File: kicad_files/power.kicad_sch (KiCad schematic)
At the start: 20 parts, among them J8 Conn_01x02_Socket, Q1 FDMC510P-MS, U11 LT1963AxST-3.3, U12 AP63205WU

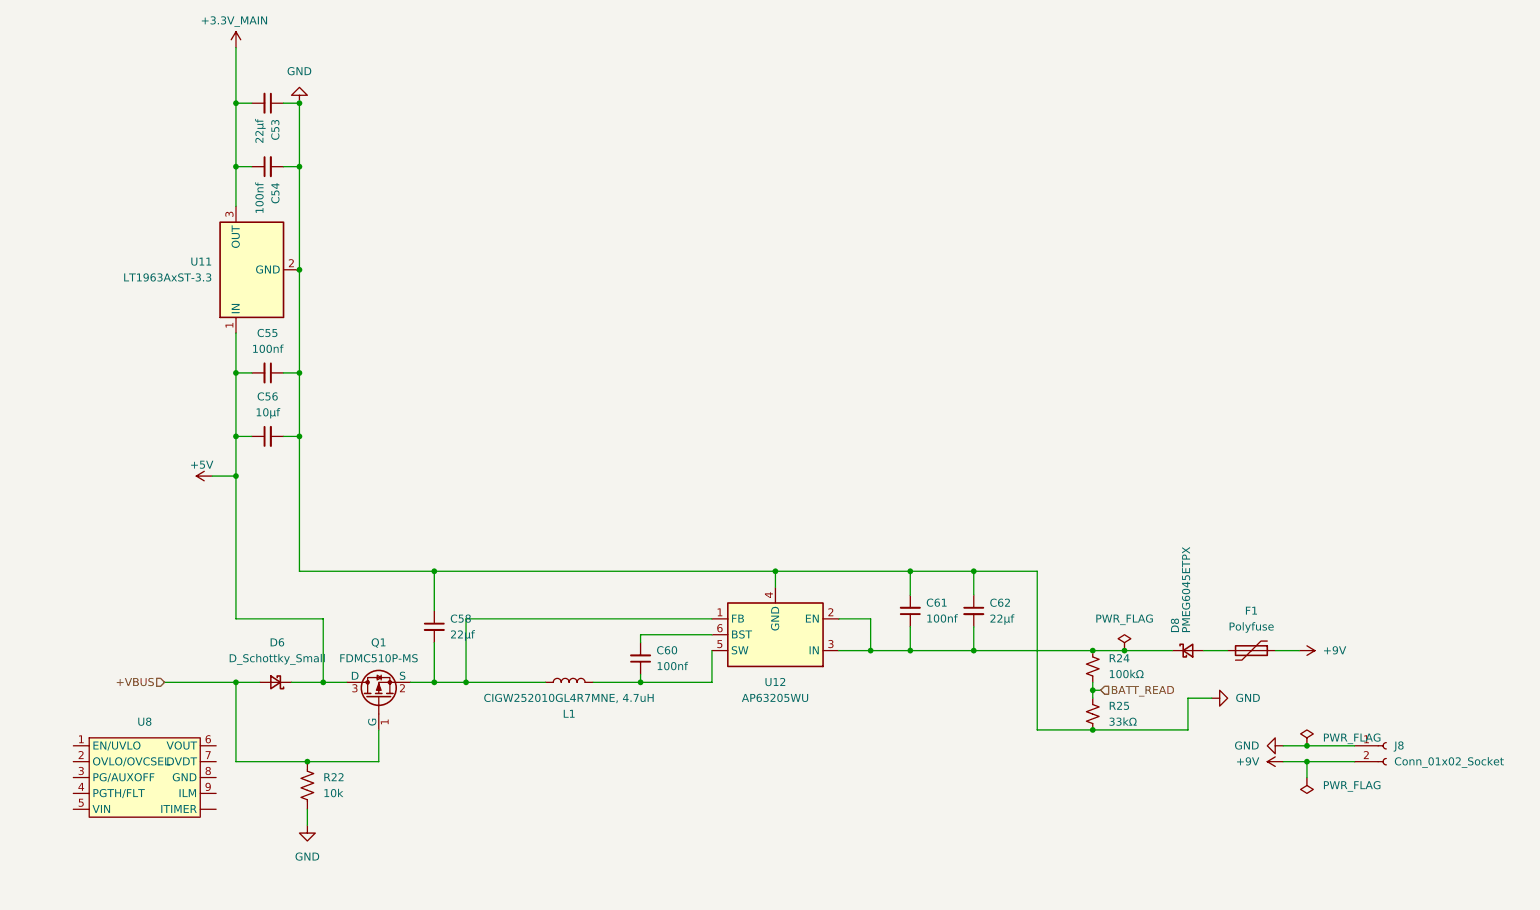
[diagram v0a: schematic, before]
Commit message: add dedicated power switching
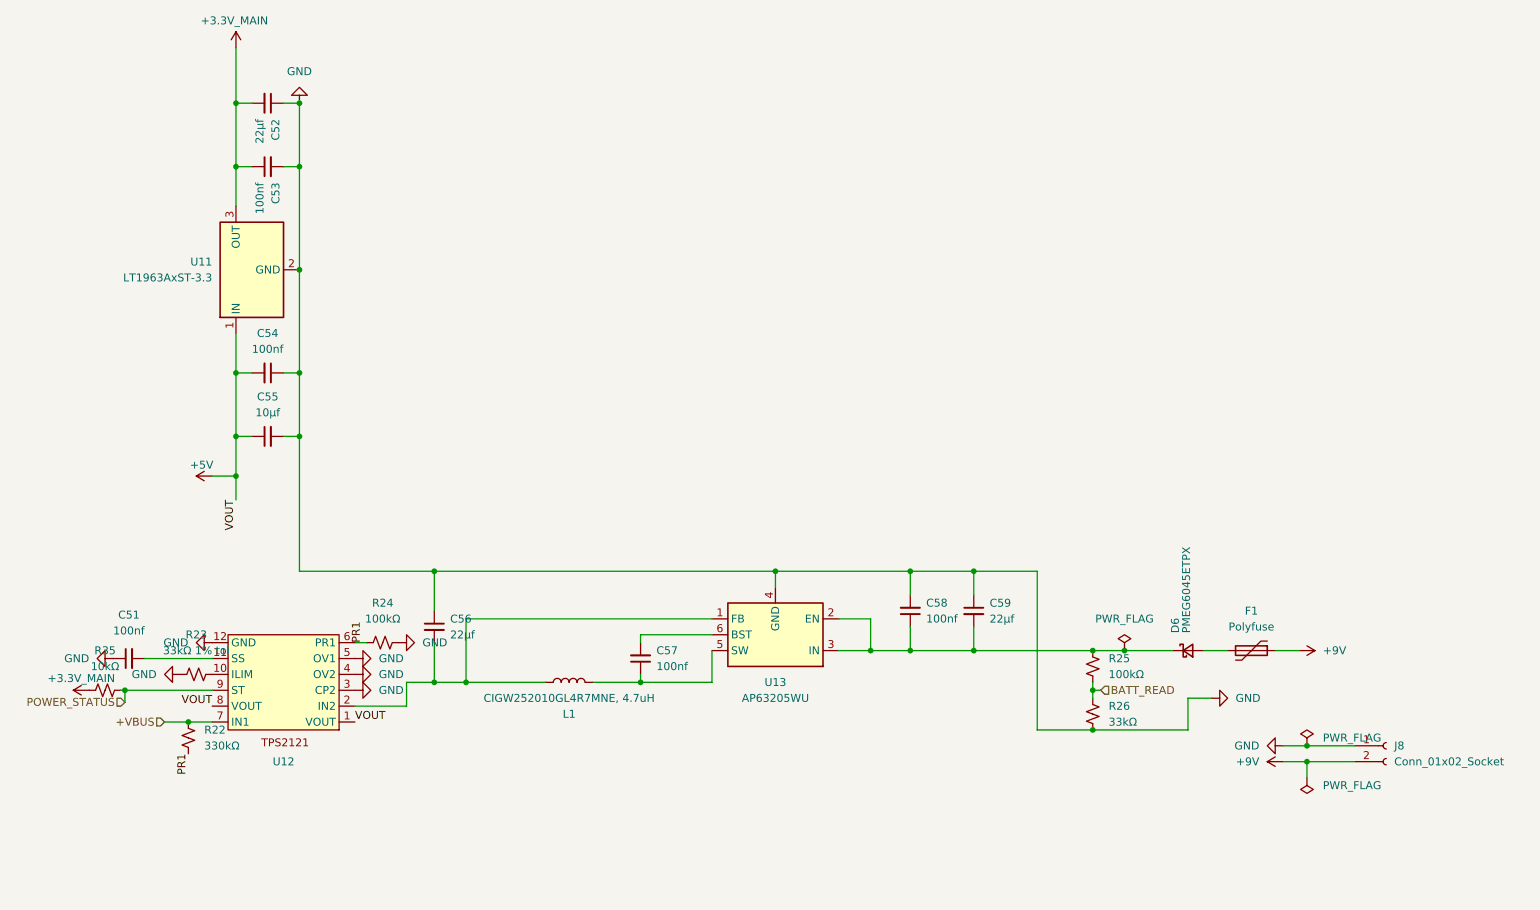
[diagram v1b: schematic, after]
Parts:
- removed D6: D_Schottky_Small, symbol Device:D_Schottky_Small
- removed Q1: FDMC510P-MS, Package_DFN_QFN:DFN-8-1EP_3x3mm_P0.65mm_EP1.6x2.56mm_ThermalVias, symbol Transistor_FET:Q_PMOS_GSD
- removed R22: 10k, Resistor_SMD:R_0402_1005Metric, symbol Device:R_US
- added C51: 100nf, Capacitor_SMD:C_0402_1005Metric, symbol Device:C_Small
- added R22: 330kΩ, Resistor_SMD:R_0402_1005Metric, symbol Device:R_Small_US
- added R23: 33kΩ 1% tol, Resistor_SMD:R_0402_1005Metric, symbol Device:R_Small_US
- added R24: 100kΩ, Resistor_SMD:R_0402_1005Metric, symbol Device:R_Small_US
- added R35: 10kΩ, Resistor_SMD:R_0402_1005Metric, symbol Device:R_Small_US
- U12: renamed from U8; footprint footprints:IC_TPS25974ARPWR -> footprints:IC_TPS2121RUXR
- renumbered C53 to C52, C54 to C53, C55 to C54, C56 to C55, C58 to C56, C60 to C57, C61 to C58, C62 to C59, D8 to D6, R24 to R25, R25 to R26, U12 to U13
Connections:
- net +3.3V_MAIN: now also R35.1
- net +5V: now also U12.1 (VOUT), U12.8 (VOUT)
- net +VBUS: now also U12.7 (IN1), R22.2
- net GND: now also U12.12 (GND), U12.3 (CP2), U12.4 (OV2), U12.5 (OV1), C51.1, R23.1, R24.2
- net at U12.2 (IN2): now also C56.2, L1.1, U13.1 (FB)
- net PR1: now reaches U12.6 (PR1)
- net PR1: now also R22.1, R24.1
- net POWER_STATUS: now reaches U12.9 (ST)
- net POWER_STATUS: now also R35.2
- new net: R23.2, U12.10 (ILIM)
- new net: C51.2, U12.11 (SS)

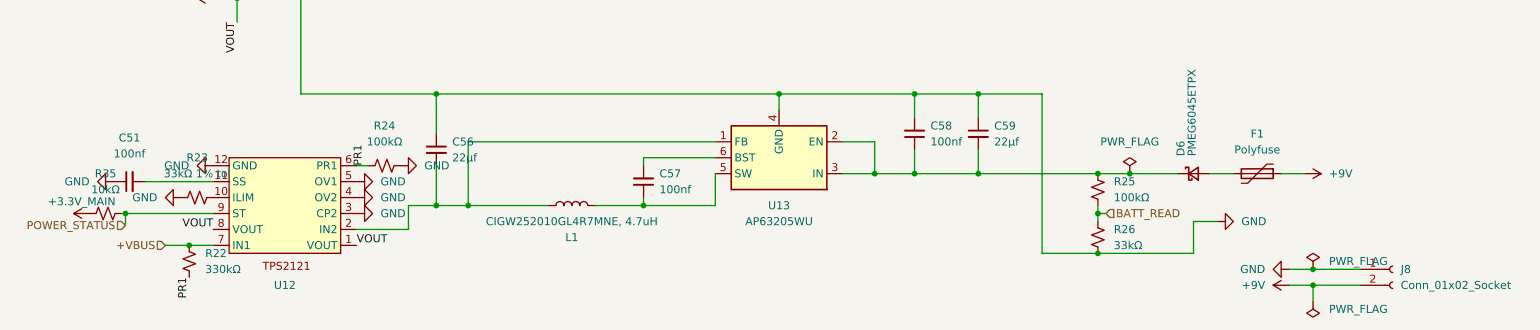
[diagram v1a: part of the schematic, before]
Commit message: size polyfuse, final drc stuff
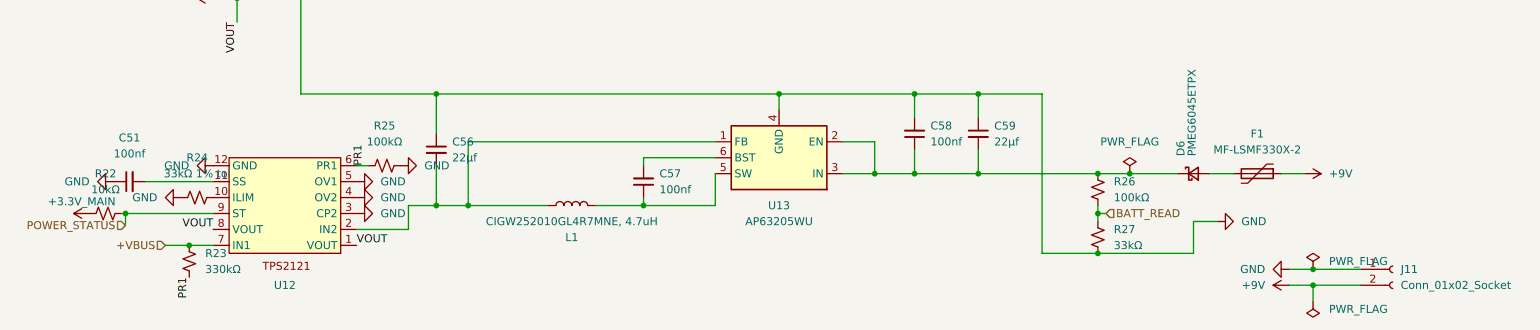
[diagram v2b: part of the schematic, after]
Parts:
- F1: value Polyfuse -> MF-LSMF330X-2; footprint Fuse:Fuse_1812_4532Metric -> Fuse:Fuse_Bourns_MF-SM_7.98x5.44mm
- renumbered J8 to J11, R35 to R22, R22 to R23, R23 to R24, R24 to R25, R25 to R26, R26 to R27
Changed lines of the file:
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@@
 		(dnp no)
 		(fields_autoplaced yes)
-		(property "Reference" "#PWR092"
+		(property "Reference" "#PWR093"
 			(at 207.01 134.62 0)
 			(hide yes)
@@
 			(project "versorlite"
 				(path "/1a230af0-0a74-48f7-8607-b087121dda49/31c1824a-552d-4de4-ae9b-4526af07be04"
-					(reference "#PWR092")
+					(reference "#PWR093")
 					(unit 1)
 				)
@@
 		(dnp no)
 		(fields_autoplaced yes)
-		(property "Reference" "#PWR091"
+		(property "Reference" "#PWR092"
 			(at 212.09 152.4 0)
 			(hide yes)
@@
 			(project "versorlite"
 				(path "/1a230af0-0a74-48f7-8607-b087121dda49/31c1824a-552d-4de4-ae9b-4526af07be04"
-					(reference "#PWR091")
+					(reference "#PWR092")
 					(unit 1)
 				)
@@
 			)
 		)
-		(property "Value" "Polyfuse"
+		(property "Value" "MF-LSMF330X-2"
 			(at 203.2 130.81 90)
 			(show_name no)
@@
 			)
 		)
-		(property "Footprint" "Fuse:Fuse_1812_4532Metric"
+		(property "Footprint" "Fuse:Fuse_Bourns_MF-SM_7.98x5.44mm"
 			(at 198.12 135.89 0)
 			(hide yes)
@@
 		(dnp no)
 		(fields_autoplaced yes)
-		(property "Reference" "#PWR080"
+		(property "Reference" "#PWR081"
 			(at 25.4 138.43 0)
 			(hide yes)
@@
 			(project "versorlite"
 				(path "/1a230af0-0a74-48f7-8607-b087121dda49/31c1824a-552d-4de4-ae9b-4526af07be04"
-					(reference "#PWR080")
+					(reference "#PWR081")
 					(unit 1)
 				)
@@
 		(dnp no)
 		(fields_autoplaced yes)
-		(property "Reference" "R26"
+		(property "Reference" "R27"
 			(at 180.34 143.5099 0)
 			(show_name no)
@@
 			(project "versorlite"
 				(path "/1a230af0-0a74-48f7-8607-b087121dda49/31c1824a-552d-4de4-ae9b-4526af07be04"
-					(reference "R26")
+					(reference "R27")
 					(unit 1)
 				)
@@
 		(dnp no)
 		(fields_autoplaced yes)
-		(property "Reference" "#PWR090"
+		(property "Reference" "#PWR091"
 			(at 201.93 149.86 0)
 			(hide yes)
@@
 			(project "versorlite"
 				(path "/1a230af0-0a74-48f7-8607-b087121dda49/31c1824a-552d-4de4-ae9b-4526af07be04"
-					(reference "#PWR090")
+					(reference "#PWR091")
 					(unit 1)
 				)
@@
 		(in_pos_files yes)
 		(dnp no)
-		(property "Reference" "#PWR085"
+		(property "Reference" "#PWR086"
 			(at 66.04 135.89 0)
 			(hide yes)
@@
 			(project "versorlite"
 				(path "/1a230af0-0a74-48f7-8607-b087121dda49/31c1824a-552d-4de4-ae9b-4526af07be04"
-					(reference "#PWR085")
+					(reference "#PWR086")
 					(unit 1)
 				)
@@
 		(dnp no)
 		(fields_autoplaced yes)
-		(property "Reference" "#PWR087"
+		(property "Reference" "#PWR088"
 			(at 66.04 140.97 0)
 			(hide yes)
@@
 			(project "versorlite"
 				(path "/1a230af0-0a74-48f7-8607-b087121dda49/31c1824a-552d-4de4-ae9b-4526af07be04"
-					(reference "#PWR087")
+					(reference "#PWR088")
 					(unit 1)
 				)
@@
 		(in_pos_files yes)
 		(dnp no)
-		(property "Reference" "#PWR0101"
+		(property "Reference" "#PWR079"
 			(at 20.955 140.97 0)
 			(hide yes)
@@
 			(project "versorlite"
 				(path "/1a230af0-0a74-48f7-8607-b087121dda49/31c1824a-552d-4de4-ae9b-4526af07be04"
-					(reference "#PWR0101")
+					(reference "#PWR079")
 					(unit 1)
 				)
@@
 		(dnp no)
 		(fields_autoplaced yes)
-		(property "Reference" "R35"
+		(property "Reference" "R22"
 			(at 19.685 134.62 90)
 			(show_name no)
@@
 			(project "versorlite"
 				(path "/1a230af0-0a74-48f7-8607-b087121dda49/31c1824a-552d-4de4-ae9b-4526af07be04"
-					(reference "R35")
+					(reference "R22")
 					(unit 1)
 				)
@@
 		(dnp no)
 		(fields_autoplaced yes)
-		(property "Reference" "J8"
+		(property "Reference" "J11"
 			(at 226.06 149.8599 0)
 			(show_name no)
@@
 			(project "versorlite"
 				(path "/1a230af0-0a74-48f7-8607-b087121dda49/31c1824a-552d-4de4-ae9b-4526af07be04"
-					(reference "J8")
+					(reference "J11")
 					(unit 1)
 				)
@@
 		(dnp no)
 		(fields_autoplaced yes)
-		(property "Reference" "#PWR084"
+		(property "Reference" "#PWR085"
 			(at 50.8 40.64 0)
 			(hide yes)
@@
 			(project "versorlite"
 				(path "/1a230af0-0a74-48f7-8607-b087121dda49/31c1824a-552d-4de4-ae9b-4526af07be04"
-					(reference "#PWR084")
+					(reference "#PWR085")
 					(unit 1)
 				)
@@
 		(dnp no)
 		(fields_autoplaced yes)
-		(property "Reference" "R23"
+		(property "Reference" "R24"
 			(at 34.29 132.08 90)
 			(show_name no)
@@
 			(project "versorlite"
 				(path "/1a230af0-0a74-48f7-8607-b087121dda49/31c1824a-552d-4de4-ae9b-4526af07be04"
-					(reference "R23")
+					(reference "R24")
 					(unit 1)
 				)
@@
 		(dnp no)
 		(fields_autoplaced yes)
-		(property "Reference" "R24"
+		(property "Reference" "R25"
 			(at 64.135 127 90)
 			(show_name no)
@@
 			(project "versorlite"
 				(path "/1a230af0-0a74-48f7-8607-b087121dda49/31c1824a-552d-4de4-ae9b-4526af07be04"
-					(reference "R24")
+					(reference "R25")
 					(unit 1)
 				)
@@
 		(in_pos_files yes)
 		(dnp no)
-		(property "Reference" "#PWR088"
+		(property "Reference" "#PWR089"
 			(at 73.025 133.35 0)
 			(hide yes)
@@
 			(project "versorlite"
 				(path "/1a230af0-0a74-48f7-8607-b087121dda49/31c1824a-552d-4de4-ae9b-4526af07be04"
-					(reference "#PWR088")
+					(reference "#PWR089")
 					(unit 1)
 				)
@@
 		(in_pos_files yes)
 		(dnp no)
-		(property "Reference" "#PWR079"
+		(property "Reference" "#PWR080"
 			(at 14.605 135.89 0)
 			(hide yes)
@@
 			(project "versorlite"
 				(path "/1a230af0-0a74-48f7-8607-b087121dda49/31c1824a-552d-4de4-ae9b-4526af07be04"
-					(reference "#PWR079")
+					(reference "#PWR080")
 					(unit 1)
 				)
@@
 		(in_pos_files yes)
 		(dnp no)
-		(property "Reference" "#PWR082"
+		(property "Reference" "#PWR083"
 			(at 30.48 133.35 0)
 			(hide yes)
@@
 			(project "versorlite"
 				(path "/1a230af0-0a74-48f7-8607-b087121dda49/31c1824a-552d-4de4-ae9b-4526af07be04"
-					(reference "#PWR082")
+					(reference "#PWR083")
 					(unit 1)
 				)
@@
 		(dnp no)
 		(fields_autoplaced yes)
-		(property "Reference" "#PWR089"
+		(property "Reference" "#PWR090"
 			(at 203.2 142.24 0)
 			(hide yes)
@@
 			(project "versorlite"
 				(path "/1a230af0-0a74-48f7-8607-b087121dda49/31c1824a-552d-4de4-ae9b-4526af07be04"
-					(reference "#PWR089")
+					(reference "#PWR090")
 					(unit 1)
 				)
@@
 		(dnp no)
 		(fields_autoplaced yes)
-		(property "Reference" "R22"
+		(property "Reference" "R23"
 			(at 35.56 147.3199 0)
 			(show_name no)
@@
 			(project "versorlite"
 				(path "/1a230af0-0a74-48f7-8607-b087121dda49/31c1824a-552d-4de4-ae9b-4526af07be04"
-					(reference "R22")
+					(reference "R23")
 					(unit 1)
 				)
@@
 		(in_pos_files yes)
 		(dnp no)
-		(property "Reference" "#PWR081"
+		(property "Reference" "#PWR082"
 			(at 40.64 106.68 0)
 			(hide yes)
@@
 			(project "versorlite"
 				(path "/1a230af0-0a74-48f7-8607-b087121dda49/31c1824a-552d-4de4-ae9b-4526af07be04"
-					(reference "#PWR081")
+					(reference "#PWR082")
 					(unit 1)
 				)
@@
 		(in_pos_files yes)
 		(dnp no)
-		(property "Reference" "#PWR086"
+		(property "Reference" "#PWR087"
 			(at 66.04 138.43 0)
 			(hide yes)
@@
 			(project "versorlite"
 				(path "/1a230af0-0a74-48f7-8607-b087121dda49/31c1824a-552d-4de4-ae9b-4526af07be04"
-					(reference "#PWR086")
+					(reference "#PWR087")
 					(unit 1)
 				)
@@
 		(dnp no)
 		(fields_autoplaced yes)
-		(property "Reference" "R25"
+		(property "Reference" "R26"
 			(at 180.34 135.8899 0)
 			(show_name no)
@@
 			(project "versorlite"
 				(path "/1a230af0-0a74-48f7-8607-b087121dda49/31c1824a-552d-4de4-ae9b-4526af07be04"
-					(reference "R25")
+					(reference "R26")
 					(unit 1)
 				)
@@
 		(in_pos_files yes)
 		(dnp no)
-		(property "Reference" "#PWR083"
+		(property "Reference" "#PWR084"
 			(at 40.64 41.91 0)
 			(hide yes)
@@
 			(project "versorlite"
 				(path "/1a230af0-0a74-48f7-8607-b087121dda49/31c1824a-552d-4de4-ae9b-4526af07be04"
-					(reference "#PWR083")
+					(reference "#PWR084")
 					(unit 1)
 				)

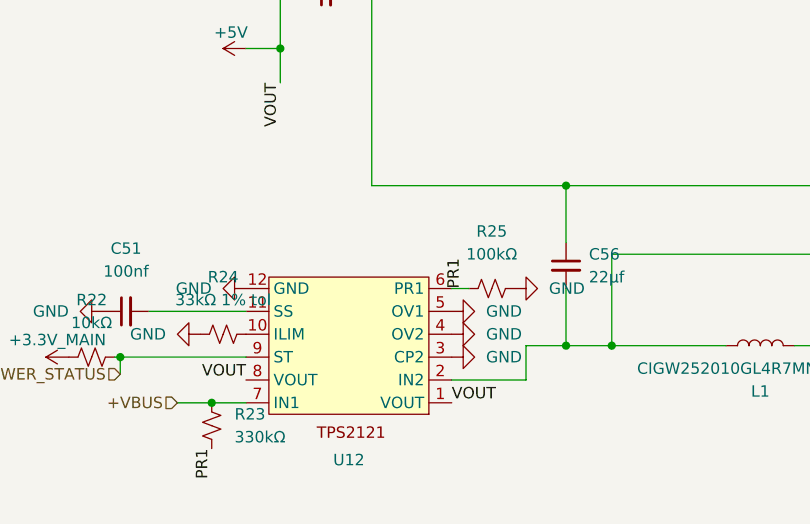
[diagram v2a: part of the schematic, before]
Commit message: fix thermal vias
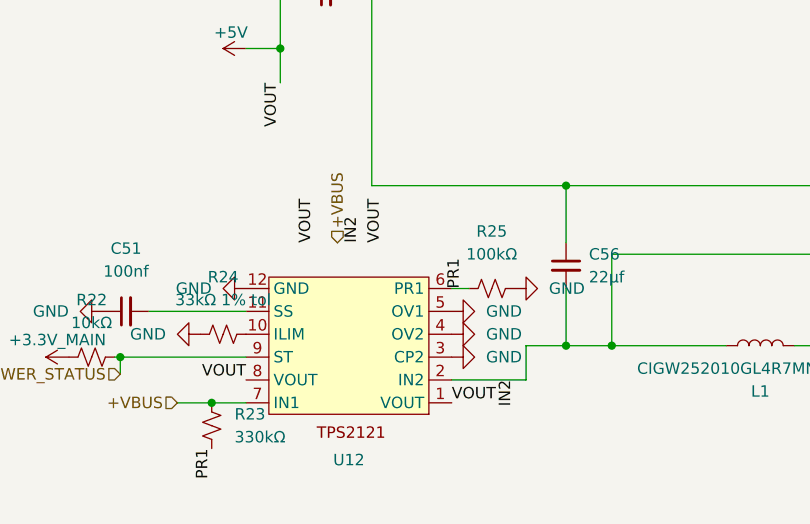
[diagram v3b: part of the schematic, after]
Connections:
- net +5V: now also U12.1_1 (TV), U12.8_1 (TV)
- net +VBUS: now also U12.7_1 (TV)
- net IN2: now reaches C56.2, L1.1, U12.2 (IN2), U13.1 (FB)
- net IN2: now also U12.2_1 (TV)
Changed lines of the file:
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@@
+		)
+	)
+	(label "IN2"
+		(at 66.675 143.51 270)
+		(effects
+			(font
+				(size 1.27 1.27)
+			)
+			(justify right bottom)
+		)
+	)
+	(label "VOUT"
+		(at 44.45 128.27 90)
+		(effects
+			(font
+				(size 1.27 1.27)
+			)
+			(justify left bottom)
+		)
+	)
+	(label "IN2"
+		(at 49.53 128.27 90)
+		(effects
+			(font
+				(size 1.27 1.27)
+			)
+			(justify left bottom)
 		)
 	)
@@
 			)
 			(justify right bottom)
+		)
+	)
+	(label "VOUT"
+		(at 52.07 128.27 90)
+		(effects
+			(font
+				(size 1.27 1.27)
+			)
+			(justify left bottom)
 		)
 	)
@@
 			)
 			(justify right)
+		)
+	)
+	(hierarchical_label "+VBUS"
+		(shape input)
+		(at 46.99 128.27 90)
+		(effects
+			(font
+				(size 1.27 1.27)
+			)
+			(justify left)
 		)
 	)
@@
 		(pin "12"
 		)
+		(pin "1_1"
+		)
+		(pin "8_1"
+		)
+		(pin "7_1"
+		)
+		(pin "2_1"
+		)
 		(instances

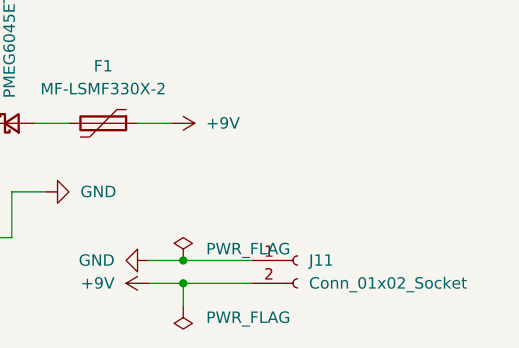
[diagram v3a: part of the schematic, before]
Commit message: better schematic labeling so that mr. dzula isn't confused
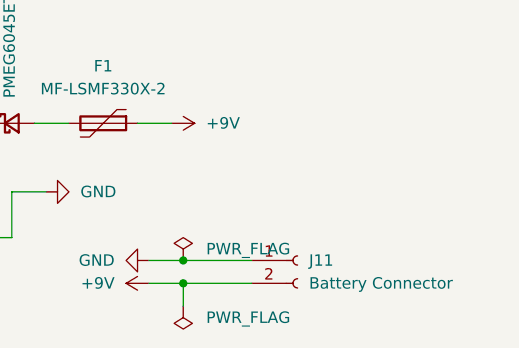
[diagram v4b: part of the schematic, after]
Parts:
- J11: value Conn_01x02_Socket -> Battery Connector
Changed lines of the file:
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@@
 			)
 		)
-		(property "Value" "Conn_01x02_Socket"
+		(property "Value" "Battery Connector"
 			(at 226.06 152.3999 0)
 			(show_name no)
